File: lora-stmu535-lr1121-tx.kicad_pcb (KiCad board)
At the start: 4 copper layers, 95.3 x 38.5 mm, 123 parts, among them J1 Conn_Coaxial_Small, J2 Conn_02x07_Odd_Even, J4 USB_C_Receptacle_USB2.0_16P, J5 2.4Ghz Antenna, J6 Conn_01x03_Pin, J7 Conn_02x06_Counter_Clockwise, SW3 SW_Push, U1 BME280, U2 BGS12WN6E6327, U3 BQ25570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

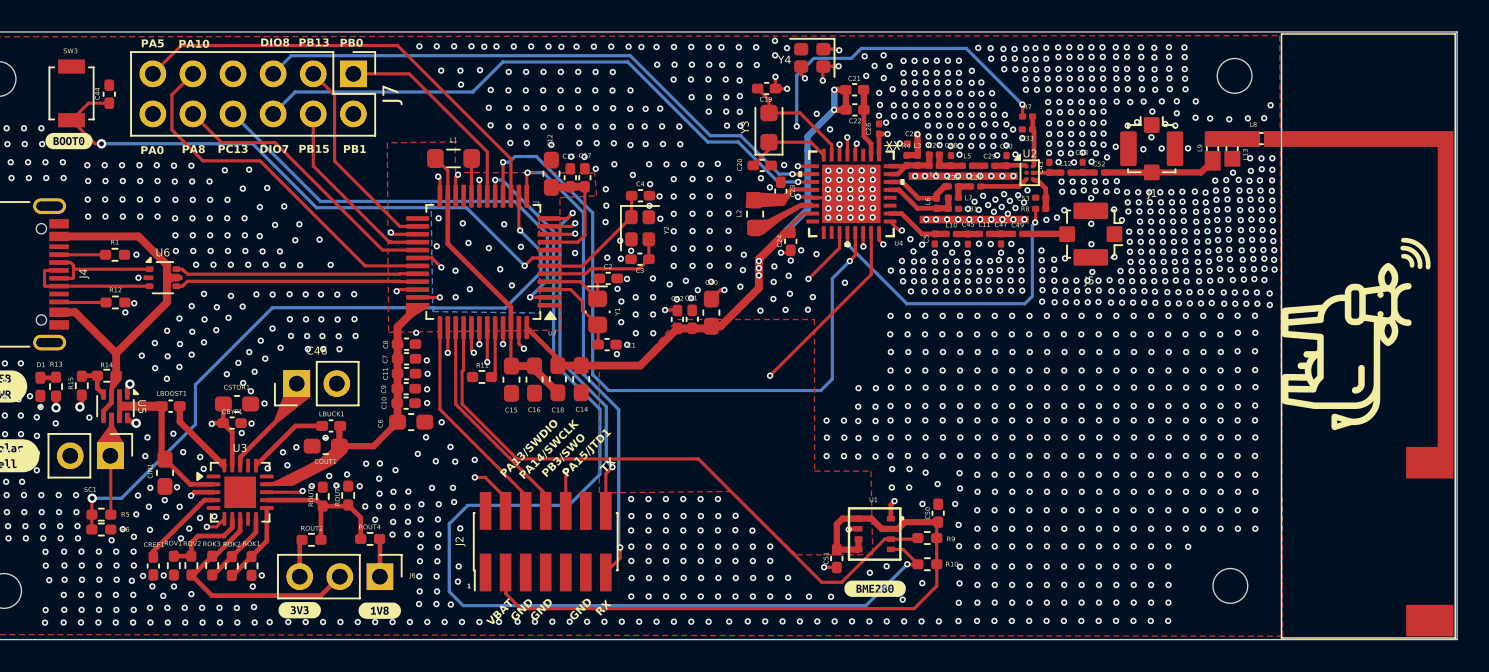
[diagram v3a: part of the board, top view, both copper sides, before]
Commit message: changed RF switch in schematics, todo in pcb
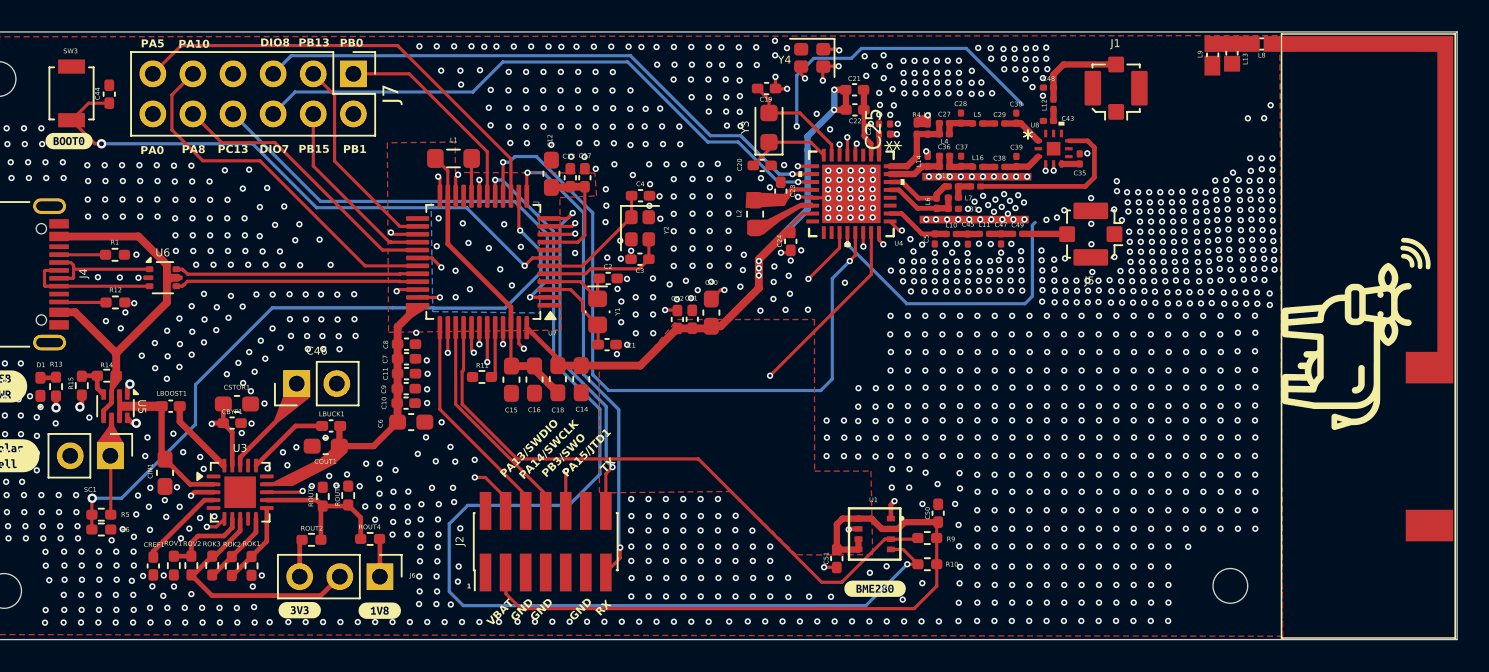
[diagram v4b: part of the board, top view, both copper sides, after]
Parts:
- removed C33, C53: 1nF, Capacitor_SMD:C_0201_0603Metric
- removed C52: 47pF, Capacitor_SMD:C_0201_0603Metric
- removed R7: 100R, Resistor_SMD:R_0201_0603Metric
- removed R8: 0R, Resistor_SMD:R_0201_0603Metric
- removed the REF** at (180.5, 54.1)
- removed U2: BGS12WN6E6327, Package_LGA:Infineon_PG-TSNP-6-10_0.7x1.1mm_0.7x1.1mm_P0.4mm
- added C35: 1nF, Capacitor_SMD:C_0201_0603Metric, F.Cu at (170.7, 59.3)
- added C36: 3.0pF, Capacitor_SMD:C_0201_0603Metric, F.Cu at (162.1, 59.1)
- added C37: 6.8pF, Capacitor_SMD:C_0201_0603Metric, F.Cu at (163.2, 59.5)
- added C38: 47pF, Capacitor_SMD:C_0201_0603Metric, F.Cu at (165.6, 59.8)
- added C39: 1.5pF, Capacitor_SMD:C_0201_0603Metric, F.Cu at (166.7, 59.5)
- added L14: 47nH, Inductor_SMD:L_0201_0603Metric, F.Cu at (161.1, 59.5)
- added L15: 2.7nH, Inductor_SMD:L_0201_0603Metric, F.Cu at (162.1, 59.8)
- added L16: 6.8nH, Inductor_SMD:L_0201_0603Metric, F.Cu at (164.2, 59.8)
- added U8: SKY13588-460LF, sky13588:QFN12_SKY-L, F.Cu at (169.0, 58.7)
- moved L13 6.05 mm to (180.3, 52.6)
- moved AE1 6.02 mm to (176.8, 51.0)
- moved L8 5.99 mm to (182.2, 52.0)
- moved L9 5.94 mm to (179.1, 52.7)
- moved C48 5.49 mm to (168.7, 54.8), turned to 0 degrees
- moved J1 4.45 mm to (173.0, 54.9), turned to 180 degrees
- moved L12 4.40 mm to (169.0, 55.9), turned to 90 degrees
- moved C43 2.94 mm to (168.7, 56.9), turned to 0 degrees
- moved C28 2.77 mm to (163.2, 56.7)
- moved C30 2.76 mm to (166.7, 56.8)
- moved L5 2.75 mm to (164.2, 57.1)
- moved C29 2.75 mm to (165.6, 57.1)
- moved L4 2.10 mm to (162.1, 57.8)
- moved C27 2.09 mm to (162.1, 57.1)
- moved R4 2.09 mm to (160.4, 57.4)
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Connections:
- net Net-(U4-RFI_N_LF0) renamed /RF/N_LF0
- net Net-(U4-RFI_P_LF0) renamed /RF/P_LF0
- AE1 pad 1: /RF/868_RF -> Net-(AE1-A)
- AE1 pad 2: GND -> (no net)
- C21 pad 2: Net-(U4-VBAT_RF) -> GND
- C22 pad 2: Net-(U4-VBAT_RF) -> GND
- C48 pad 2: Net-(C48-Pad2) -> /RF/868_RF
- L12 pad 2: Net-(C48-Pad2) -> /RF/868_RF
- U4 pad 2: Net-(U4-VBAT_RF) -> VBAT
- U4 pad 31: Net-(U4-RFO_HP_LF) -> Net-(U4-RFO_LP_LF)
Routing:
- net Net-(U8-J2): track 2.99 -> 11.1 mm
- net Net-(U4-VBAT_RF): track 4.34 -> 0.00 mm
- net (no net): track 0.00 -> 4.34 mm
- net Net-(U4-RFO_LP_LF): track 0.00 -> 4.04 mm
- net Net-(U2-CTRL): track 3.11 -> 0.00 mm
- net Net-(U8-J3): track 0.00 -> 2.39 mm
- net /RF/VR_PA: track 5.83 -> 8.15 mm, vias 2 -> 3
- net Net-(U2-VDD): track 2.25 -> 0.00 mm
- net Net-(C36-Pad2): track 0.00 -> 2.19 mm
- net Net-(C48-Pad2): track 1.49 -> 0.00 mm
- net /RF/868_RF: track 7.16 -> 5.80 mm
- net VBAT: track 106.7 -> 107.8 mm
- net Net-(U4-RFO_HP_LF): track 4.46 -> 5.49 mm
- net Net-(C38-Pad2): track 0.00 -> 0.76 mm
- net Net-(U8-JT): track 1.95 -> 2.60 mm
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
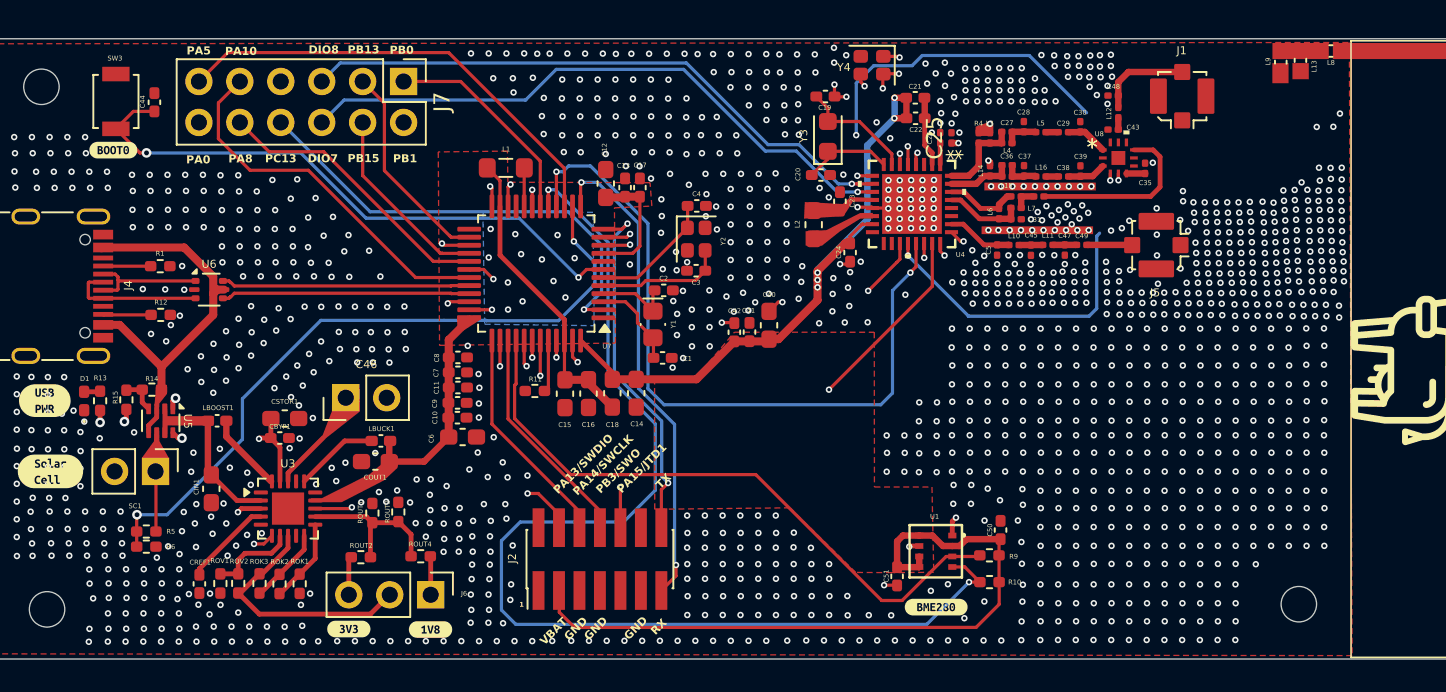
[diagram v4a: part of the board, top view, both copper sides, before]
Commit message: separated matching lines
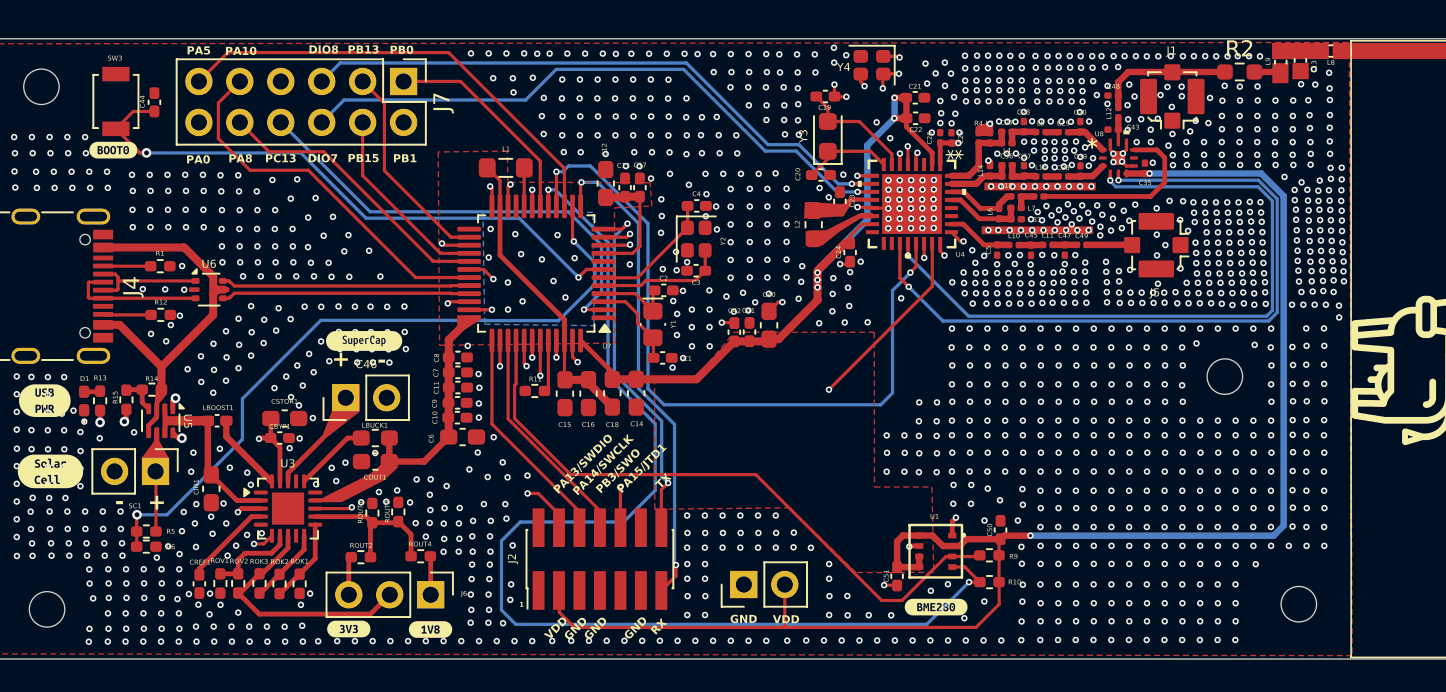
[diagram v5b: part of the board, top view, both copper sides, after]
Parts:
- added R2: 0R, Resistor_SMD:R_0603_1608Metric_Pad0.98x0.95mm_HandSolder, F.Cu at (176.6, 53.4)
- added REF**: MountingHole_2.2mm_M2, MountingHole:MountingHole_2.2mm_M2, F.Cu at (175.6, 72.2)
- added REF**: PinHeader_1x02_P2.54mm_Vertical, Connector_PinHeader_2.54mm:PinHeader_1x02_P2.54mm_Vertical, F.Cu at (145.8, 85.2)
- added kibuzzard-69EF5185: G***, kibuzzard-69EF5185, F.Cu at (122.2, 70.0)
- LBUCK1: footprint Inductor_SMD:L_0402_1005Metric_Pad0.77x0.64mm_HandSolder -> Inductor_SMD:L_0603_1608Metric_Pad1.05x0.95mm_HandSolder
- R6: value 2.13M -> 2.49M
- ROUT3: value 8.66 -> 8.66M
- ROUT4: value 4.22 -> 4.22M
- moved J1 0.62 mm to (172.4, 54.9)
- moved LBUCK1 0.39 mm to (122.9, 76.1)
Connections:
- AE1 pad 1: Net-(AE1-A) -> Net-(L9-Pad1)
- L9 pad 1: /RF/868_RF -> Net-(L9-Pad1)
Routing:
- net VBAT: track 107.8 -> 161.7 mm, vias 17 -> 19
- net /RF/RFSW0: track 19.4 -> 42.9 mm
- net /RF/RFSW1: track 34.0 -> 44.7 mm, vias 3 -> 2
- net (no net): track 4.34 -> 0.00 mm
- net GND: track 19.4 -> 22.9 mm, vias 1434 -> 1506
- net /RF/868_RF: track 5.80 -> 8.45 mm
- net Net-(L9-Pad1): track 0.00 -> 1.76 mm
- net Net-(U8-RFC): track 0.73 -> 1.53 mm
- net /RF/VR_PA: track 8.15 -> 8.85 mm
- net Net-(U3-LBUCK): track 5.23 -> 4.65 mm
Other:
- board text added: "+"
- board text added: "-"
- board text added: "VDD"
- board text removed: "VBAT"

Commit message: fix smtp line and minor errors
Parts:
- added C33: 47pF, Capacitor_SMD:C_0201_0603Metric, F.Cu at (161.7, 58.4)
- added kibuzzard-69F35B1F: G***, kibuzzard-69F35B1F, F.Cu at (132.7, 57.7)
- added kibuzzard-69F35B2E: G***, kibuzzard-69F35B2E, F.Cu at (156.0, 65.7)
- L1: value 2.2uH, 1.5A -> 2.2uH
- moved C25 3.13 mm to (161.4, 55.9), turned to 0 degrees
- moved L3 0.05 mm to (161.1, 57.4)
- moved R4 0.05 mm to (160.4, 57.4)
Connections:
- AE1 pad 2: (no net) -> GND
- AE1 pad 3: (no net) -> Net-(AE1-A)
- C18 pad 2: VDD11 -> GND
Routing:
- net VDD11: track 18.9 -> 16.8 mm
- net /RF/VR_PA: track 8.85 -> 9.74 mm
- net GND: vias 1506 -> 1519
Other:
- board text removed: "TODO: - Recheck RF"
